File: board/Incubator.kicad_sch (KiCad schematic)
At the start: 53 parts, among them J1 TFT SPI interface, J10 NTC2, J2 I2C connector, J3 RS485/DHT11, J4 Relay1, J5 VAC 230V, J6 VDC 5V, J7 Relay2, J8 FLOWMETER/NTC, J9 TX RX - +, K1 FINDER-36.11, K2 FINDER-36.11, Q1 BC547, Q2 BC547, Q3 BC847, Q4 BC847, U1 ESP32-WROOM-32, U2 MAX485E, U3 AMS1117-3.3

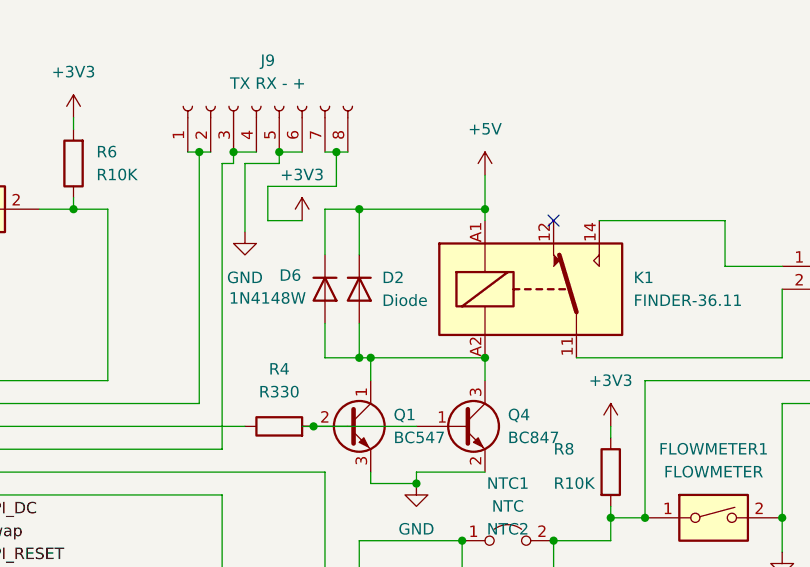
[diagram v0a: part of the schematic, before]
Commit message: [UPD] Update days and avoid wire interferences
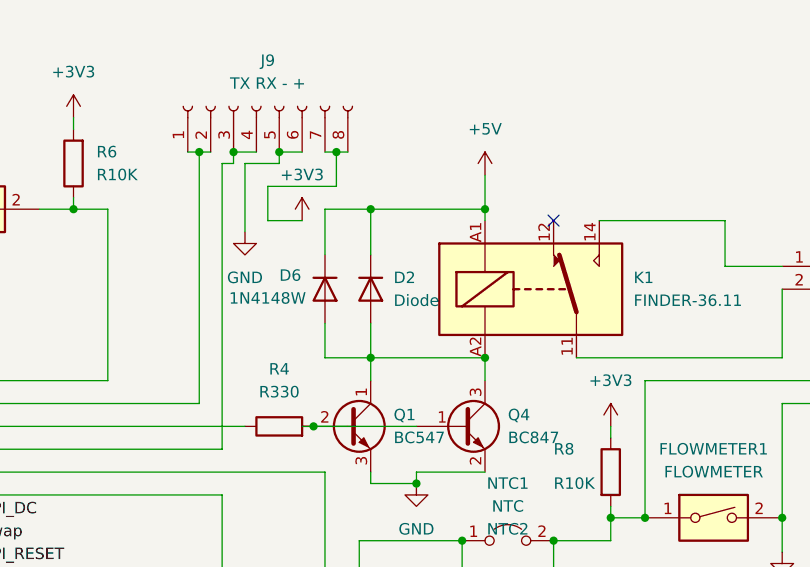
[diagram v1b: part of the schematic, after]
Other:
- moved on the sheet: D2
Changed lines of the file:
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@@
 	)
 	(junction
+		(at 148.59 38.1)
+		(diameter 0)
+		(color 0 0 0 0)
+	)
+	(junction
 		(at 66.04 172.72)
 		(diameter 0)
@@
 	)
 	(junction
-		(at 147.32 38.1)
-		(diameter 0)
-		(color 0 0 0 0)
-	)
-	(junction
 		(at 201.93 135.89)
 		(diameter 0)
@@
 	)
 	(junction
-		(at 147.32 54.61)
-		(diameter 0)
-		(color 0 0 0 0)
-	)
-	(junction
 		(at 194.31 72.39)
 		(diameter 0)
@@
 	(wire
 		(pts
-			(xy 147.32 54.61) (xy 143.51 54.61)
+			(xy 143.51 54.61) (xy 148.59 54.61)
 		)
 		(stroke
@@
 	(wire
 		(pts
-			(xy 143.51 38.1) (xy 147.32 38.1)
+			(xy 143.51 38.1) (xy 148.59 38.1)
 		)
 		(stroke
@@
 	(wire
 		(pts
-			(xy 147.32 38.1) (xy 161.29 38.1)
-		)
-		(stroke
-			(width 0)
-			(type default)
-		)
-	)
-	(wire
-		(pts
 			(xy 92.71 163.83) (xy 90.17 163.83)
 		)
@@
 	(wire
 		(pts
-			(xy 148.59 54.61) (xy 147.32 54.61)
-		)
-		(stroke
-			(width 0)
-			(type default)
-		)
-	)
-	(wire
-		(pts
 			(xy 132.08 181.61) (xy 132.08 182.88)
 		)
@@
 	(wire
 		(pts
+			(xy 148.59 38.1) (xy 161.29 38.1)
+		)
+		(stroke
+			(width 0)
+			(type default)
+		)
+	)
+	(wire
+		(pts
 			(xy 143.51 54.61) (xy 143.51 50.8)
 		)
@@
 	(wire
 		(pts
-			(xy 147.32 50.8) (xy 147.32 54.61)
+			(xy 148.59 50.8) (xy 148.59 54.61)
 		)
 		(stroke
@@
 	(wire
 		(pts
-			(xy 147.32 43.18) (xy 147.32 38.1)
+			(xy 148.59 43.18) (xy 148.59 38.1)
 		)
 		(stroke
@@
 	(symbol
 		(lib_id "Diode:1N5400")
-		(at 147.32 46.99 270)
+		(at 148.59 46.99 270)
 		(unit 1)
 		(exclude_from_sim no)
@@
 		(fields_autoplaced yes)
 		(property "Reference" "D2"
-			(at 149.86 45.72 90)
+			(at 151.13 45.72 90)
 			(effects
 				(font
@@
 		)
 		(property "Value" "Diode"
-			(at 149.86 48.26 90)
+			(at 151.13 48.26 90)
 			(effects
 				(font
@@
 		)
 		(property "Footprint" "Diode_THT:D_DO-35_SOD27_P10.16mm_Horizontal"
-			(at 142.875 46.99 0)
+			(at 144.145 46.99 0)
 			(effects
 				(font
@@
 		)
 		(property "Datasheet" ""
-			(at 147.32 46.99 0)
+			(at 148.59 46.99 0)
 			(effects
 				(font
@@
 		)
 		(property "Description" ""
-			(at 147.32 46.99 0)
+			(at 148.59 46.99 0)
 			(effects
 				(font
@@
 		)
 		(property "Sim.Device" "D"
-			(at 147.32 46.99 0)
+			(at 148.59 46.99 0)
 			(effects
 				(font
@@
 		)
 		(property "Sim.Pins" "1=K 2=A"
-			(at 147.32 46.99 0)
+			(at 148.59 46.99 0)
 			(effects
 				(font
